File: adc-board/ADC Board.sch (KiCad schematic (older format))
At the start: 58 parts, among them J2 ST-LINK/V2, J3 USART1, J4 USART6, J5 UE27AC5410H, J7 AltPowerInput, J8 USBPowerJumper, U0 STM32H743ZITx, U10 MCP1501-20E/SN, U13 3.3V Reg, U9 USBLC6-2SC6, Y1 NX3225GD-8.000M-EXS00A-CG04874

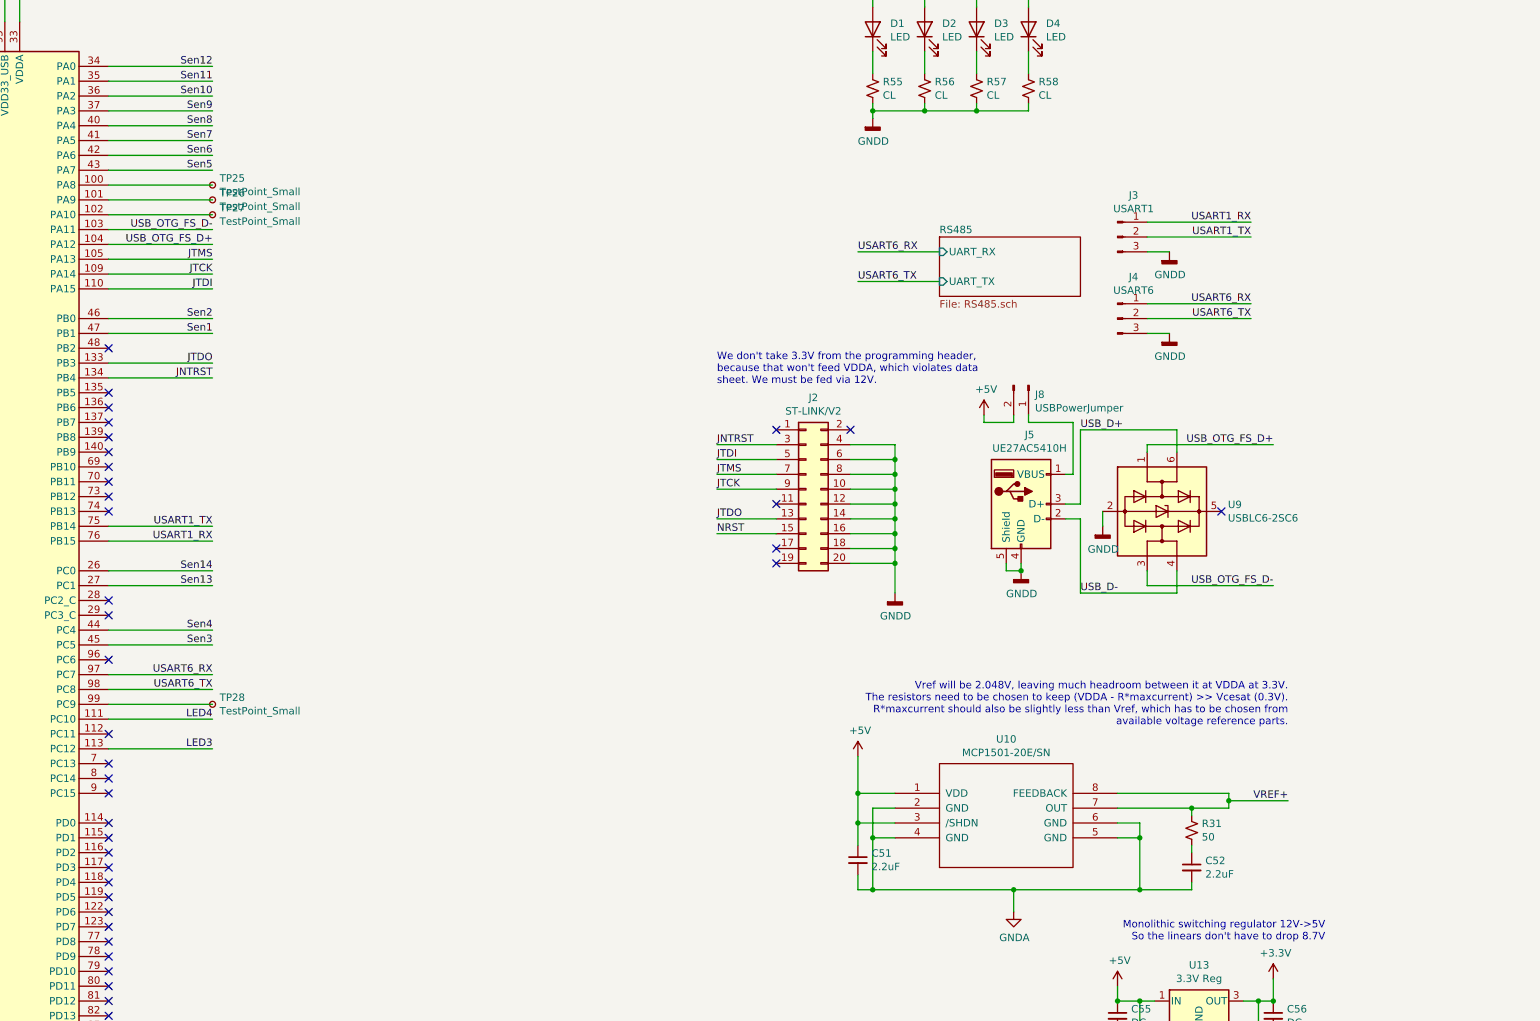
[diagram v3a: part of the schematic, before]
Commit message: USB VBUS sensing; rearrange/correct USARTs
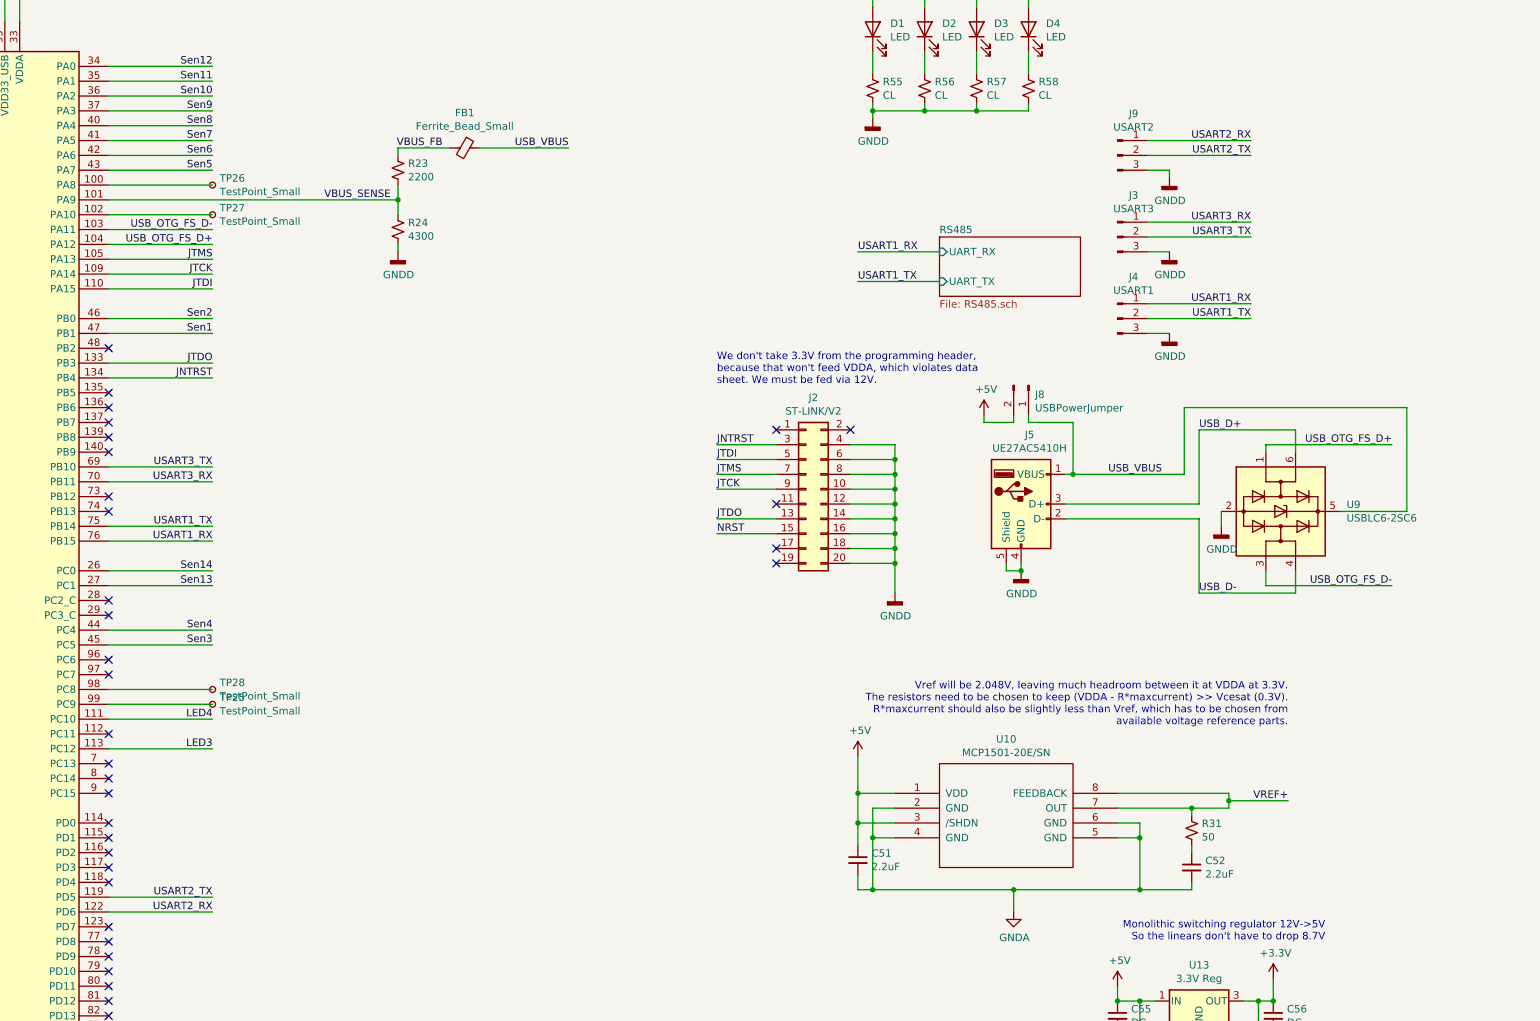
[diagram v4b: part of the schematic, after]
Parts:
- added FB1: Ferrite_Bead_Small, Inductors_SMD:L_0805, symbol Device:Ferrite_Bead_Small
- added J9: USART2, Pin_Headers:Pin_Header_Straight_1x03_Pitch2.54mm, symbol Connector:Conn_01x03_Male
- added R23: 2200, Resistors_SMD:R_0805, symbol Device:R_Small_US
- added R24: 4300, Resistors_SMD:R_0805, symbol Device:R_Small_US
- J3: value USART1 -> USART3
- J4: value USART6 -> USART1
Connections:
- net GNDD: now also J9.3 (Pin_3), R24.2
- net USART1_RX: now also J4.1 (Pin_1); no longer J3.1 (Pin_1)
- net USART1_TX: now also J4.2 (Pin_2); no longer J3.2 (Pin_2)
- net at U0.100 (PA8): now also TP26.1; no longer TP25.1
- net VBUS_SENSE: now reaches U0.101 (PA9)
- net VBUS_SENSE: now also R23.2, R24.1; no longer TP26.1
- net USART2_TX: now reaches U0.119 (PD5)
- net USART2_TX: now also J9.2 (Pin_2)
- net USART2_RX: now reaches U0.122 (PD6)
- net USART2_RX: now also J9.1 (Pin_1)
- net USART3_TX: now reaches U0.69 (PB10)
- net USART3_TX: now also J3.2 (Pin_2)
- net USART3_RX: now reaches U0.70 (PB11)
- net USART3_RX: now also J3.1 (Pin_1)
- net at TP28.1: now also U0.98 (PC8); no longer U0.99 (PC9)
- net USB_VBUS: now reaches J5.1 (VBUS), J8.1 (Pin_1)
- net USB_VBUS: now also U9.5 (VBUS), FB1.1
- net USART6_RX: no longer names the net of U0.97 (PC7)
- net USART6_RX: no longer J4.1 (Pin_1)
- removed net USART6_TX: J4.2 (Pin_2), U0.98 (PC8)
- new net: TP25.1, U0.99 (PC9)
- new net VBUS_FB: FB1.2, R23.1
- no-connect marks 75 -> 71
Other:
- moved on the sheet: TP25, TP26, TP28, U9
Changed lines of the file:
@@
 	6350 5550 7050 5550
-Wire Wire Line
-	6350 6450 7050 6450
 Wire Wire Line
 	6350 6550 7050 6550
@@
 Text Label 7050 5550 2    50   ~ 0
 USART1_RX
-Text Label 7050 6450 2    50   ~ 0
-USART6_RX
-Text Label 7050 6550 2    50   ~ 0
-USART6_TX
 Text Label 7050 6150 2    50   ~ 0
 Sen4
@@
 Text Label 7050 5850 2    50   ~ 0
 Sen13
-Wire Wire Line
-	12800 5300 12900 5300
-Wire Wire Line
-	12800 5400 12900 5400
 $Comp
 L power:GNDD #PWR0113
@@
 P 13150 3500
 F 0 "J3" H 13258 3781 50  0000 C CNN
-F 1 "USART1" H 13258 3690 50  0000 C CNN
+F 1 "USART3" H 13258 3690 50  0000 C CNN
 F 2 "Pin_Headers:Pin_Header_Straight_1x03_Pitch2.54mm" H 13150 3500 50  0001 C CNN
 F 3 "~" H 13150 3500 50  0001 C CNN
@@
 P 13150 4050
 F 0 "J4" H 13258 4331 50  0000 C CNN
-F 1 "USART6" H 13258 4240 50  0000 C CNN
+F 1 "USART1" H 13258 4240 50  0000 C CNN
 F 2 "Pin_Headers:Pin_Header_Straight_1x03_Pitch1.27mm" H 13150 4050 50  0001 C CNN
 F 3 "~" H 13150 4050 50  0001 C CNN
@@
 $EndComp
 Text Label 14050 3400 2    50   ~ 0
+USART3_RX
+Text Label 14050 3500 2    50   ~ 0
+USART3_TX
+Text Label 14050 3950 2    50   ~ 0
 USART1_RX
-Text Label 14050 3500 2    50   ~ 0
+Text Label 14050 4050 2    50   ~ 0
 USART1_TX
-Text Label 14050 3950 2    50   ~ 0
-USART6_RX
-Text Label 14050 4050 2    50   ~ 0
-USART6_TX
 $Comp
 L Device:C C32
@@
 L Power_Protection:USBLC6-2SC6 U9
 U 1 1 606C142F
-P 13450 5350
-F 0 "U9" V 13404 5794 50  0000 L CNN
-F 1 "USBLC6-2SC6" V 13495 5794 50  0000 L CNN
-F 2 "TO_SOT_Packages_SMD:SOT-23-6_Handsoldering" H 13450 4850 50  0001 C CNN
-F 3 "https://www.st.com/resource/en/datasheet/usblc6-2.pdf" H 13650 5700 50  0001 C CNN
-	1    13450 5350
+P 14250 5350
+F 0 "U9" V 14204 5794 50  0000 L CNN
+F 1 "USBLC6-2SC6" V 14295 5794 50  0000 L CNN
+F 2 "TO_SOT_Packages_SMD:SOT-23-6_Handsoldering" H 14250 4850 50  0001 C CNN
+F 3 "https://www.st.com/resource/en/datasheet/usblc6-2.pdf" H 14450 5700 50  0001 C CNN
+	1    14250 5350
 	0    1    1    0
 $EndComp
@@
 L power:GNDD #PWR0122
 U 1 1 607593F4
-P 13050 5450
-F 0 "#PWR0122" H 13050 5200 50  0001 C CNN
-F 1 "GNDD" H 13054 5295 50  0000 C CNN
-F 2 "" H 13050 5450 50  0001 C CNN
-F 3 "" H 13050 5450 50  0001 C CNN
-	1    13050 5450
-	1    0    0    -1
-$EndComp
-Wire Wire Line
-	12900 5400 12900 5900
-Wire Wire Line
-	12900 5300 12900 4800
+P 13850 5450
+F 0 "#PWR0122" H 13850 5200 50  0001 C CNN
+F 1 "GNDD" H 13854 5295 50  0000 C CNN
+F 2 "" H 13850 5450 50  0001 C CNN
+F 3 "" H 13850 5450 50  0001 C CNN
+	1    13850 5450
+	1    0    0    -1
+$EndComp
+Wire Wire Line
+	13700 5400 13700 5900
+Wire Wire Line
+	13700 5300 13700 4800
 Wire Wire Line
 	12500 5750 12500 5700
-Text Label 12900 4800 0    50   ~ 0
+Text Label 13700 4800 0    50   ~ 0
 USB_D+
-Text Label 12900 5900 0    50   ~ 0
+Text Label 13700 5900 0    50   ~ 0
 USB_D-
 Wire Wire Line
-	13050 5450 13050 5350
-Wire Wire Line
-	13550 4800 13550 4950
-Wire Wire Line
-	12900 4800 13550 4800
-Wire Wire Line
-	13550 5900 13550 5750
-Wire Wire Line
-	12900 5900 13550 5900
-Wire Wire Line
-	13350 5750 13350 5850
-Wire Wire Line
-	13350 5850 14200 5850
-Wire Wire Line
-	13350 4950 13350 4900
-Wire Wire Line
-	13350 4900 14200 4900
-Text Label 14200 4900 2    50   ~ 0
+	13850 5450 13850 5350
+Wire Wire Line
+	14350 4800 14350 4950
+Wire Wire Line
+	13700 4800 14350 4800
+Wire Wire Line
+	14350 5900 14350 5750
+Wire Wire Line
+	13700 5900 14350 5900
+Wire Wire Line
+	14150 5750 14150 5850
+Wire Wire Line
+	14150 5850 15000 5850
+Wire Wire Line
+	14150 4950 14150 4900
+Wire Wire Line
+	14150 4900 15000 4900
+Text Label 15000 4900 2    50   ~ 0
 USB_OTG_FS_D+
-Text Label 14200 5850 2    50   ~ 0
+Text Label 15000 5850 2    50   ~ 0
 USB_OTG_FS_D-
 Wire Wire Line
@@
 	11950 3800 11400 3800
 Text Label 11400 3600 0    50   ~ 0
-USART6_RX
+USART1_RX
 Text Label 11400 3800 0    50   ~ 0
-USART6_TX
+USART1_TX
 $Comp
 L Device:LED D1
@@
 	6350 6650 7050 6650
 Wire Wire Line
-	6350 3250 7050 3250
-Wire Wire Line
 	6350 3350 7050 3350
 Wire Wire Line
@@
 L Connector:TestPoint_Small TP28
 U 1 1 63DD487F
+P 7050 6550
+F 0 "TP28" H 7098 6596 50  0000 L CNN
+F 1 "TestPoint_Small" H 7098 6505 50  0000 L CNN
+F 2 "Testpoint:TestPoint_Pad_D1.5mm" H 7250 6550 50  0001 C CNN
+F 3 "~" H 7250 6550 50  0001 C CNN
+	1    7050 6550
+	1    0    0    -1
+$EndComp
+$Comp
+L Connector:TestPoint_Small TP25
+U 1 1 63DD5CA6
 P 7050 6650
-F 0 "TP28" H 7098 6696 50  0000 L CNN
+F 0 "TP25" H 7098 6696 50  0000 L CNN
 F 1 "TestPoint_Small" H 7098 6605 50  0000 L CNN
 F 2 "Testpoint:TestPoint_Pad_D1.5mm" H 7250 6650 50  0001 C CNN
@@
 $EndComp
 $Comp
-L Connector:TestPoint_Small TP25
-U 1 1 63DD5CA6
+L Connector:TestPoint_Small TP26
+U 1 1 63DD7687
 P 7050 3150
-F 0 "TP25" H 7098 3196 50  0000 L CNN
+F 0 "TP26" H 7098 3196 50  0000 L CNN
 F 1 "TestPoint_Small" H 7098 3105 50  0000 L CNN
 F 2 "Testpoint:TestPoint_Pad_D1.5mm" H 7250 3150 50  0001 C CNN
 F 3 "~" H 7250 3150 50  0001 C CNN
 	1    7050 3150
-	1    0    0    -1
-$EndComp
-$Comp
-L Connector:TestPoint_Small TP26
-U 1 1 63DD7687
-P 7050 3250
-F 0 "TP26" H 7098 3296 50  0000 L CNN
-F 1 "TestPoint_Small" H 7098 3205 50  0000 L CNN
-F 2 "Testpoint:TestPoint_Pad_D1.5mm" H 7250 3250 50  0001 C CNN
-F 3 "~" H 7250 3250 50  0001 C CNN
-	1    7050 3250
 	1    0    0    -1
 $EndComp
@@
 NoConn ~ 6350 7750
 NoConn ~ 6350 7850
-NoConn ~ 6350 7950
-NoConn ~ 6350 8050
 NoConn ~ 6350 8150
 NoConn ~ 6350 8250
@@
 NoConn ~ 3850 5250
 NoConn ~ 3850 5350
-NoConn ~ 3850 5450
 NoConn ~ 3850 5550
 NoConn ~ 3850 5750
@@
 NoConn ~ 6350 6050
 NoConn ~ 6350 5950
-NoConn ~ 6350 5050
 NoConn ~ 6350 4950
 NoConn ~ 6350 4850
@@
 	1    0    0    -1
 $EndComp
-NoConn ~ 6350 5150
 NoConn ~ 6350 5250
 NoConn ~ 6350 5350
@@
 NoConn ~ 10850 5600
 NoConn ~ 10850 5700
-NoConn ~ 13850 5350
 $Comp
 L power:PWR_FLAG #FLG0104
@@
 	1    0    0    -1
 $EndComp
+Wire Wire Line
+	12800 5300 13700 5300
+Wire Wire Line
+	12800 5400 13700 5400
+Connection ~ 12850 5100
+Text Label 13450 5100 2    50   ~ 0
+USB_VBUS
+Wire Wire Line
+	6350 3250 8300 3250
+$Comp
+L Device:R_Small_US R24
+U 1 1 5FBFA2EB
+P 8300 3450
+F 0 "R24" H 8368 3496 50  0000 L CNN
+F 1 "4300" H 8368 3405 50  0000 L CNN
+F 2 "Resistors_SMD:R_0805" H 8300 3450 50  0001 C CNN
+F 3 "~" H 8300 3450 50  0001 C CNN
+	1    8300 3450
+	1    0    0    -1
+$EndComp
+$Comp
+L Device:R_Small_US R23
+U 1 1 5FBFAEF2
+P 8300 3050
+F 0 "R23" H 8368 3096 50  0000 L CNN
+F 1 "2200" H 8368 3005 50  0000 L CNN
+F 2 "Resistors_SMD:R_0805" H 8300 3050 50  0001 C CNN
+F 3 "~" H 8300 3050 50  0001 C CNN
+	1    8300 3050
+	1    0    0    -1
+$EndComp
+Wire Wire Line
+	8300 3150 8300 3250
+Connection ~ 8300 3250
+Wire Wire Line
+	8300 3250 8300 3350
+Wire Wire Line
+	8300 3550 8300 3600
+Wire Wire Line
+	8300 2950 8300 2900
+Wire Wire Line
+	8300 2900 8650 2900
+$Comp
+L power:GNDD #PWR0145
+U 1 1 5FC74AD6
+P 8300 3600
+F 0 "#PWR0145" H 8300 3350 50  0001 C CNN
+F 1 "GNDD" H 8304 3445 50  0000 C CNN
+F 2 "" H 8300 3600 50  0001 C CNN
+F 3 "" H 8300 3600 50  0001 C CNN
+	1    8300 3600
+	1    0    0    -1
+$EndComp
+$Comp
+L Device:Ferrite_Bead_Small FB1
+U 1 1 5FC76527
+P 8750 2900
+F 0 "FB1" V 8513 2900 50  0000 C CNN
+F 1 "Ferrite_Bead_Small" V 8604 2900 50  0000 C CNN
+F 2 "Inductors_SMD:L_0805" V 8680 2900 50  0001 C CNN
+F 3 "~" H 8750 2900 50  0001 C CNN
+	1    8750 2900
+	0    1    1    0
+$EndComp
+Wire Wire Line
+	8850 2900 9450 2900
+Text Label 9450 2900 2    50   ~ 0
+USB_VBUS
+Text Label 8250 3250 2    50   ~ 0
+VBUS_SENSE
+Text Label 8600 2900 2    50   ~ 0
+VBUS_FB
+NoConn ~ 6350 6450
+NoConn ~ 3850 5450
+Wire Wire Line
+	6350 5150 7050 5150
+Wire Wire Line
+	6350 5050 7050 5050
+Text Label 7050 5050 2    50   ~ 0
+USART3_TX
+Text Label 7050 5150 2    50   ~ 0
+USART3_RX
+Wire Wire Line
+	6350 8050 7050 8050
+Wire Wire Line
+	6350 7950 7050 7950
+Text Label 7050 8050 2    50   ~ 0
+USART2_RX
+Text Label 7050 7950 2    50   ~ 0
+USART2_TX
+$Comp
+L Connector:Conn_01x03_Male J9
+U 1 1 5FDB45DC
+P 13150 2950
+F 0 "J9" H 13258 3231 50  0000 C CNN
+F 1 "USART2" H 13258 3140 50  0000 C CNN
+F 2 "Pin_Headers:Pin_Header_Straight_1x03_Pitch2.54mm" H 13150 2950 50  0001 C CNN
+F 3 "~" H 13150 2950 50  0001 C CNN
+	1    13150 2950
+	1    0    0    -1
+$EndComp
+$Comp
+L power:GNDD #PWR0146
+U 1 1 5FDB4E6F
+P 13500 3100
+F 0 "#PWR0146" H 13500 2850 50  0001 C CNN
+F 1 "GNDD" H 13504 2945 50  0000 C CNN
+F 2 "" H 13500 3100 50  0001 C CNN
+F 3 "" H 13500 3100 50  0001 C CNN
+	1    13500 3100
+	1    0    0    -1
+$EndComp
+Wire Wire Line
+	13350 3050 13500 3050
+Wire Wire Line
+	13500 3050 13500 3100
+Wire Wire Line
+	13350 2950 14050 2950
+Wire Wire Line
+	13350 2850 14050 2850
+Text Label 14050 2850 2    50   ~ 0
+USART2_RX
+Text Label 14050 2950 2    50   ~ 0
+USART2_TX
+Wire Wire Line
+	13600 5100 13600 4650
+Wire Wire Line
+	13600 4650 15100 4650
+Wire Wire Line
+	15100 4650 15100 5350
+Wire Wire Line
+	15100 5350 14650 5350
+Wire Wire Line
+	12850 5100 13600 5100
 $EndSCHEMATC
